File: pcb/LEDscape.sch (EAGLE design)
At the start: 41 parts, among them IC1 MAX3040CSE, IC2 MAX3040CSE, IC3 MAX3040CSE, IC4 MAX3040CSE, IC5 MAX3040CSE, IC6 MAX3040CSE, IC7 MAX3040CSE, IC8 MAX3040CSE

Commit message: Update board to use 2x8 RJ45 connector
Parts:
- removed CN1, CN10, CN11, CN12, CN13, CN14, CN15, CN16, CN17, CN18, CN19, CN2, CN20, CN21, CN22, CN23, CN24, CN25, CN26, CN27, CN28, CN29, CN3, CN30, CN31, CN32, CN4, CN5, CN6, CN7, CN8, CN9: (no value), adafruit:JST_2PIN-SMT
- added U$10, U$3, U$4, U$5, U$6, U$7, U$8, U$9: RJ45_8X2_JACK, LEDscape:RJ45_8X2_JACK
- added U$2: RJ45_8X2_BASE, LEDscape:RJ45_8X2_BASE
- IC1, IC2, IC3, IC4, IC5, IC6, IC7, IC8: value MAX3040CSE -> MAX3041CUE; device maxim:MAX3040CSE -> maxim:MAX3041CUE
- U$1: value BEAGLEBONE_OUTLINE -> BEAGLEBONE_NO_OUTLINE; device adafruit:BEAGLEBONE_OUTLINE -> LEDscape:BEAGLEBONE_NO_OUTLINE
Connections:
- removed net N$57: CN28.1, IC7.Y4
- removed net N$66: CN32.2, IC8.Z4
- new net N$11: IC6.Z2, U$7.P$6
- new net N$14: IC3.Z2, U$5.P$6
- net GND: now also U$10.P$15, U$10.P$16, U$10.P$7, U$10.P$8, U$3.P$15, U$3.P$16, U$3.P$7, U$3.P$8, U$4.P$15, U$4.P$16, U$4.P$7, U$4.P$8, U$5.P$15, U$5.P$16, U$5.P$7, U$5.P$8, U$6.P$15, U$6.P$16, U$6.P$7, U$6.P$8, U$7.P$15, U$7.P$16, U$7.P$7, U$7.P$8, U$8.P$15, U$8.P$16, U$8.P$7, U$8.P$8, U$9.P$15, U$9.P$16, U$9.P$7, U$9.P$8
- net N$1: now also U$3.P$1; no longer CN1.1
- net N$10: now also U$4.P$2; no longer CN5.2
- net N$12: now also U$4.P$3; no longer CN6.1
- net N$13: now also U$4.P$6; no longer CN6.2
- net N$15: now also U$4.P$9; no longer CN7.1
- net N$16: now also U$4.P$10; no longer CN7.2
- net N$17: now also U$4.P$11; no longer CN8.1
- net N$18: now also U$4.P$14; no longer CN8.2
- net N$19: now also U$5.P$1; no longer CN9.1
- net N$2: now also U$3.P$2; no longer CN1.2
- net N$20: now also U$5.P$2; no longer CN9.2
- net N$21: now also U$5.P$3; no longer CN10.1
- net N$22: now also IC3.Z4, U$5.P$14; no longer CN10.2, IC3.Z2
- net N$23: now also U$5.P$9; no longer CN11.1
- net N$24: now also U$5.P$10; no longer CN11.2
- net N$25: now also U$5.P$11; no longer CN12.1
- net N$26: now also IC7.Y2, U$8.P$3; no longer CN12.2, IC3.Z4
- net N$27: now also U$9.P$1; no longer CN13.1
- net N$28: now also U$9.P$2; no longer CN13.2
- net N$29: now also U$9.P$3; no longer CN14.1
- net N$3: now also U$4.P$1; no longer CN5.1
- net N$30: now also U$9.P$6; no longer CN14.2
- net N$31: now also IC4.Z4, U$9.P$14; no longer CN15.1, IC4.Y3
- net N$32: now also U$9.P$10; no longer CN15.2
- net N$33: now also U$9.P$11; no longer CN16.1
- net N$34: now also IC4.Y3, U$9.P$9; no longer CN16.2, IC4.Z4
- net N$35: now also U$6.P$1; no longer CN17.1
- net N$36: now also U$6.P$2; no longer CN17.2
- net N$37: now also U$6.P$3; no longer CN18.1
- net N$38: now also U$6.P$6; no longer CN18.2
- net N$39: now also U$6.P$9; no longer CN19.1
- net N$4: now also U$3.P$3; no longer CN2.1
- net N$40: now also U$6.P$10; no longer CN19.2
- net N$41: now also U$6.P$11; no longer CN20.1
- net N$42: now also U$6.P$14; no longer CN20.2
- net N$43: now also U$7.P$1; no longer CN21.1
- net N$44: now also U$7.P$2; no longer CN21.2
- net N$45: now also U$7.P$3; no longer CN22.1
- net N$46: now also IC7.Z2, U$8.P$6; no longer CN22.2, IC6.Z2
- net N$47: now also U$7.P$9; no longer CN23.1
- net N$48: now also U$7.P$10; no longer CN23.2
- net N$49: now also U$7.P$11; no longer CN24.1
- net N$5: now also U$3.P$6; no longer CN2.2
- net N$50: now also U$7.P$14; no longer CN24.2
- net N$51: now also U$8.P$1; no longer CN25.1
- net N$52: now also U$8.P$2; no longer CN25.2
- net N$53: now also IC7.Y3, U$8.P$9; no longer CN26.1, IC7.Y2
- net N$54: now also IC7.Y4, U$8.P$11; no longer CN26.2, IC7.Z2
- net N$55: now also IC7.Z4, U$8.P$14; no longer CN27.1, IC7.Y3
- net N$56: now also U$8.P$10; no longer CN27.2
- net N$58: now also IC8.Y2, U$10.P$3; no longer CN28.2, IC7.Z4
- net N$59: now also U$10.P$1; no longer CN29.1
- net N$6: now also U$3.P$9; no longer CN3.1
- net N$60: now also U$10.P$2; no longer CN29.2
- net N$61: now also IC8.Z2, U$10.P$6; no longer CN30.1, IC8.Y2
- net N$62: now also IC8.Y4, U$10.P$11; no longer CN30.2, IC8.Z2
- net N$63: now also U$10.P$9; no longer CN31.1
- net N$64: now also U$10.P$10; no longer CN31.2
- net N$65: now also IC8.Z4, U$10.P$14; no longer CN32.1, IC8.Y4
- net N$7: now also U$3.P$10; no longer CN3.2
- net N$8: now also U$3.P$11; no longer CN4.1
- net N$9: now also U$3.P$14; no longer CN4.2
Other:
- moved on the sheet: IC2, IC3, IC4, IC6, IC7, IC8

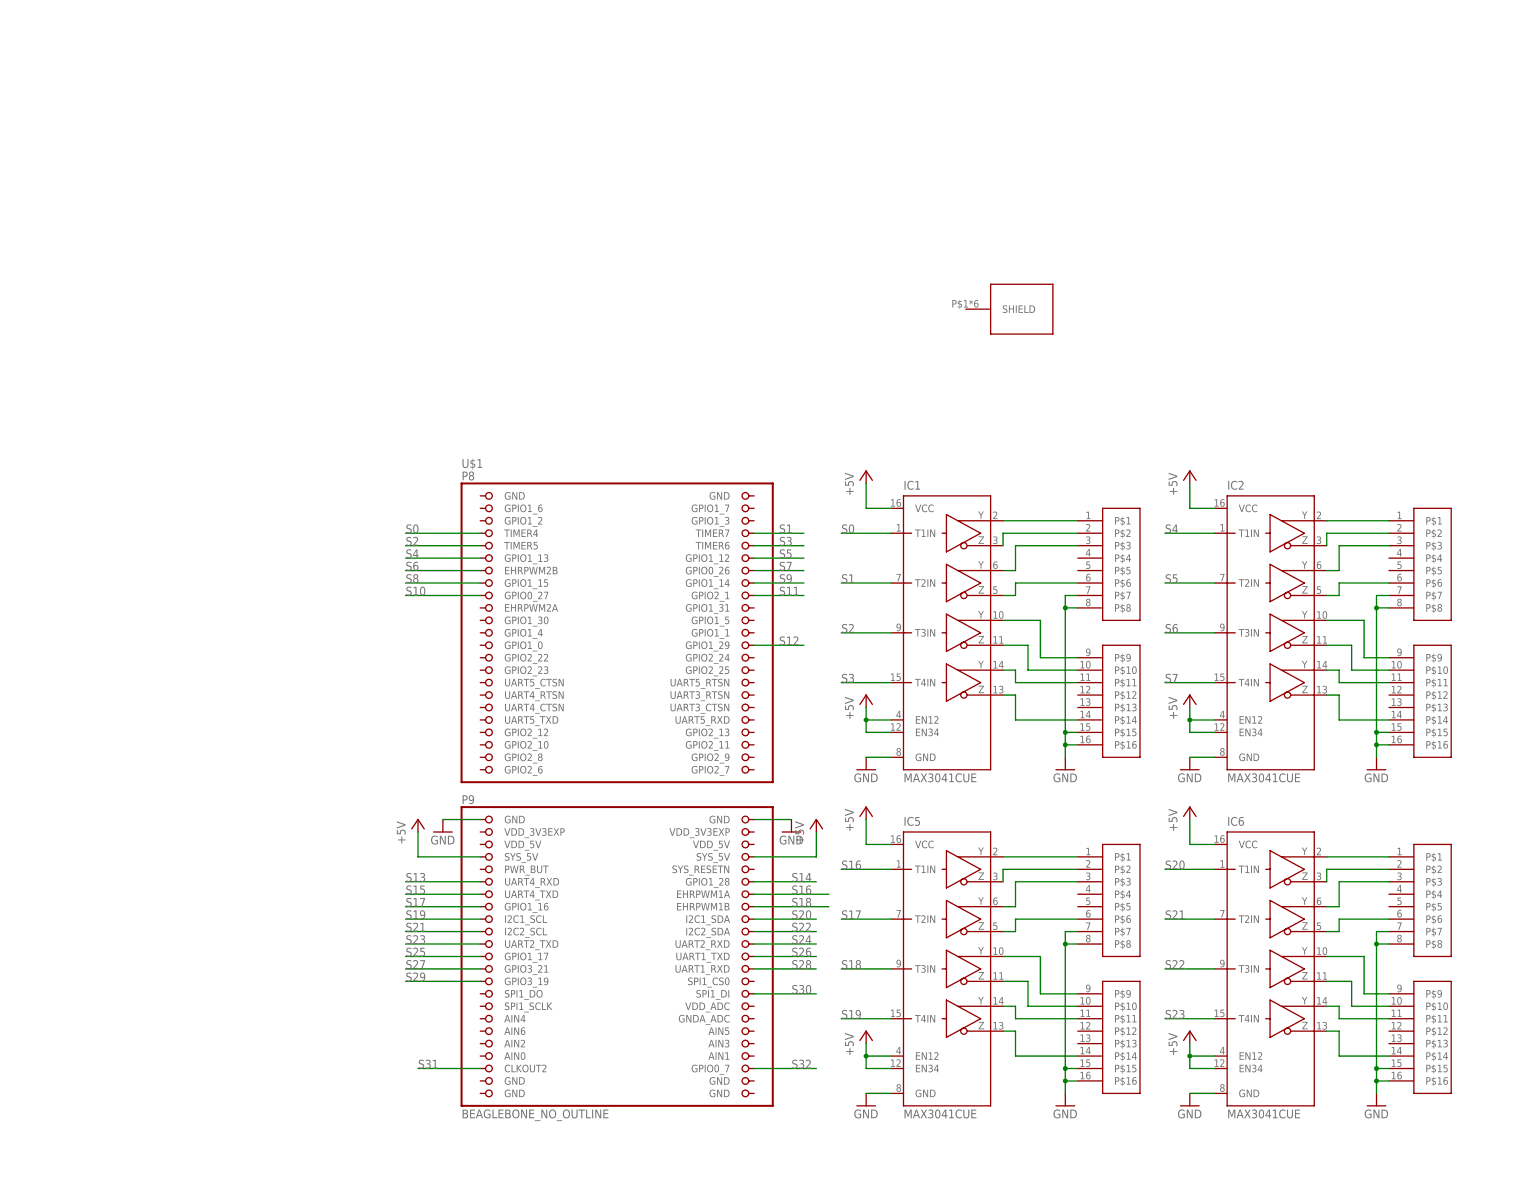
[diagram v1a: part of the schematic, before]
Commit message: Flip board over (put everything on the front, not the back), add caps, work on routing.
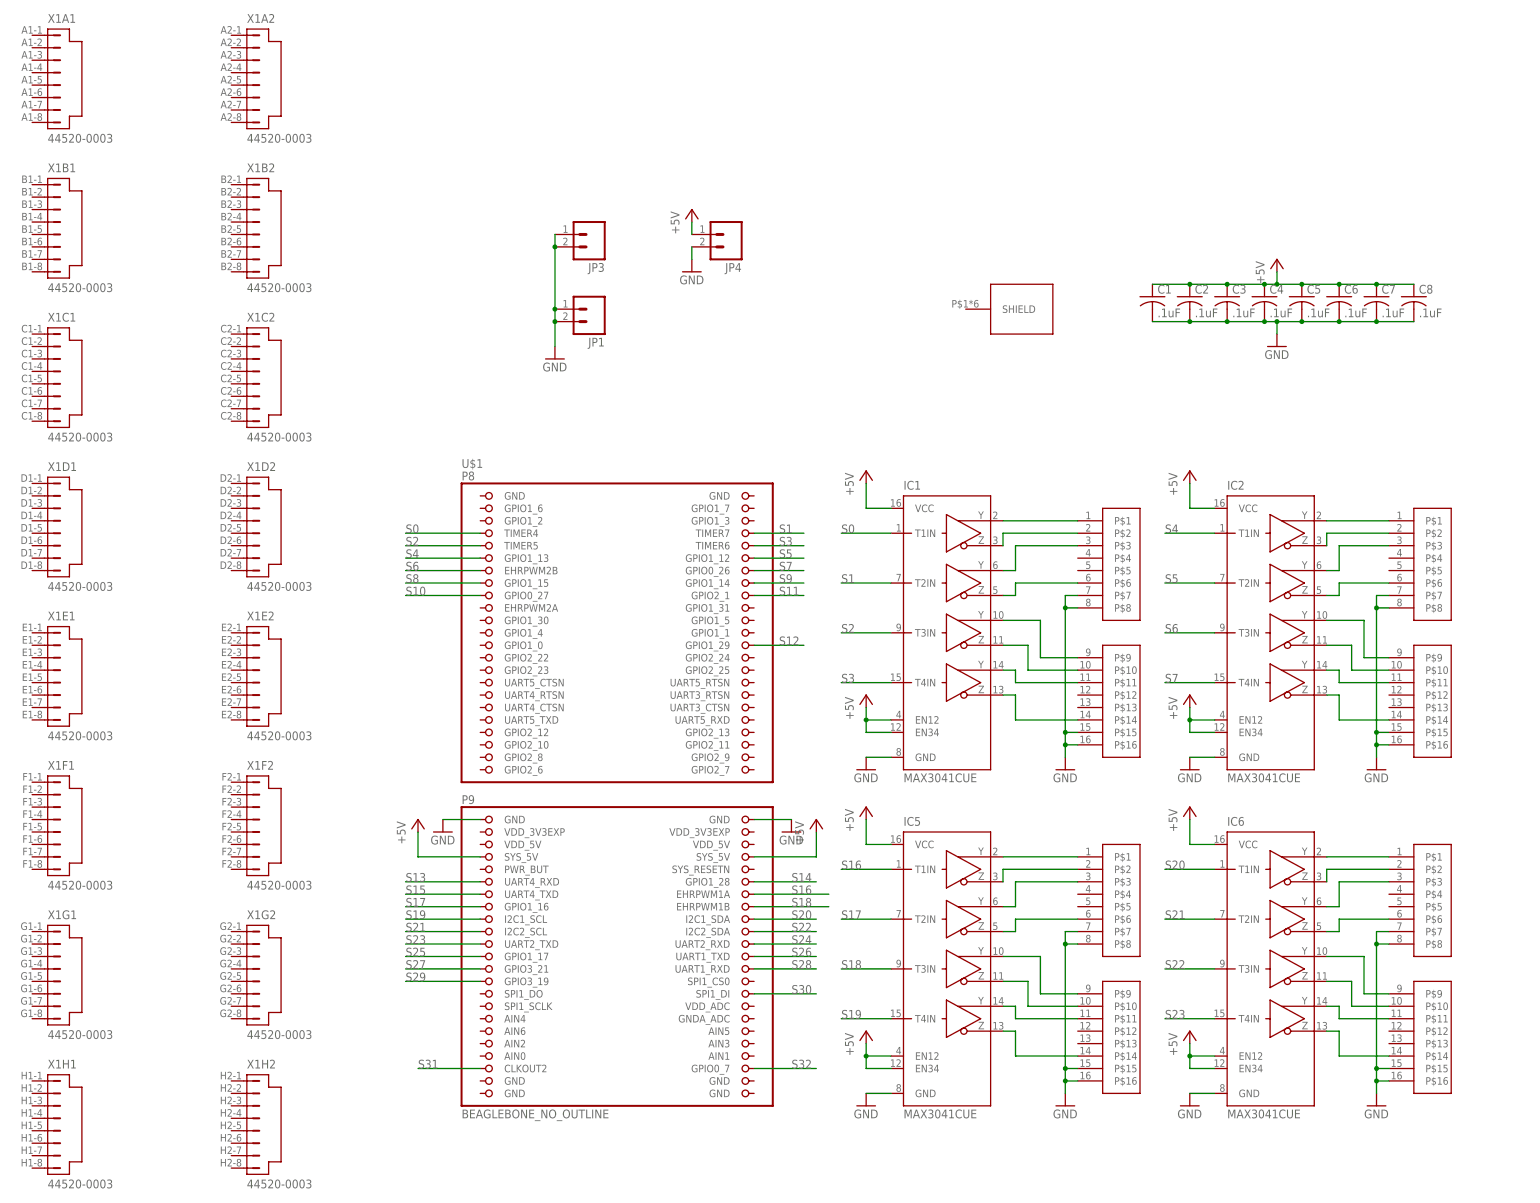
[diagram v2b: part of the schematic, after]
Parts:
- added C1, C2, C3, C4, C5, C6, C7, C8: .1uF, adafruit:C-USC0603
- added JP1, JP3, JP4: (no value), SparkFun-Connectors:M025MM
- added X1: 44520-0003, con-molex:44520-0003
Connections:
- net +5V: now also C1.1, C2.1, C3.1, C4.1, C5.1, C6.1, C7.1, C8.1, JP4.1
- net GND: now also C1.2, C2.2, C3.2, C4.2, C5.2, C6.2, C7.2, C8.2, JP1.1, JP1.2, JP3.1, JP3.2, JP4.2
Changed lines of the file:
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@@
 <part name="GND17" library="supply1" deviceset="GND" device=""/>
 <part name="GND18" library="supply1" deviceset="GND" device=""/>
+<part name="C1" library="adafruit" deviceset="C-US" device="C0603" value=".1uF"/>
+<part name="C2" library="adafruit" deviceset="C-US" device="C0603" value=".1uF"/>
+<part name="C3" library="adafruit" deviceset="C-US" device="C0603" value=".1uF"/>
+<part name="C4" library="adafruit" deviceset="C-US" device="C0603" value=".1uF"/>
+<part name="C5" library="adafruit" deviceset="C-US" device="C0603" value=".1uF"/>
+<part name="C6" library="adafruit" deviceset="C-US" device="C0603" value=".1uF"/>
+<part name="C7" library="adafruit" deviceset="C-US" device="C0603" value=".1uF"/>
+<part name="C8" library="adafruit" deviceset="C-US" device="C0603" value=".1uF"/>
+<part name="P+19" library="supply1" deviceset="+5V" device=""/>
+<part name="GND19" library="supply1" deviceset="GND" device=""/>
+<part name="X1" library="con-molex" deviceset="44520-0003" device=""/>
+<part name="JP1" library="SparkFun-Connectors" deviceset="M02" device="5MM"/>
+<part name="JP3" library="SparkFun-Connectors" deviceset="M02" device="5MM"/>
+<part name="JP4" library="SparkFun-Connectors" deviceset="M02" device="5MM"/>
+<part name="P+20" library="supply1" deviceset="+5V" device=""/>
+<part name="GND20" library="supply1" deviceset="GND" device=""/>
+<part name="GND21" library="supply1" deviceset="GND" device=""/>
 </parts>
 <sheets>
@@
 <instance part="GND17" gate="1" x="370.84" y="-27.94"/>
 <instance part="GND18" gate="1" x="370.84" y="40.64"/>
+<instance part="C1" gate="G$1" x="162.56" y="137.16"/>
+<instance part="C2" gate="G$1" x="170.18" y="137.16"/>
+<instance part="C3" gate="G$1" x="177.8" y="137.16"/>
+<instance part="C4" gate="G$1" x="185.42" y="137.16"/>
+<instance part="C5" gate="G$1" x="193.04" y="137.16"/>
+<instance part="C6" gate="G$1" x="200.66" y="137.16"/>
+<instance part="C7" gate="G$1" x="208.28" y="137.16"/>
+<instance part="C8" gate="G$1" x="215.9" y="137.16"/>
+<instance part="P+19" gate="1" x="187.96" y="144.78"/>
+<instance part="GND19" gate="1" x="187.96" y="127"/>
+<instance part="X1" gate="A1" x="-60.96" y="182.88"/>
+<instance part="X1" gate="A2" x="-20.32" y="182.88"/>
+<instance part="X1" gate="B1" x="-60.96" y="152.4"/>
+<instance part="X1" gate="B2" x="-20.32" y="152.4"/>
+<instance part="X1" gate="C1" x="-60.96" y="121.92"/>
+<instance part="X1" gate="C2" x="-20.32" y="121.92"/>
+<instance part="X1" gate="D1" x="-60.96" y="91.44"/>
+<instance part="X1" gate="D2" x="-20.32" y="91.44"/>
+<instance part="X1" gate="E1" x="-60.96" y="60.96"/>
+<instance part="X1" gate="E2" x="-20.32" y="60.96"/>
+<instance part="X1" gate="F1" x="-60.96" y="30.48"/>
+<instance part="X1" gate="F2" x="-20.32" y="30.48"/>
+<instance part="X1" gate="G1" x="-60.96" y="0"/>
+<instance part="X1" gate="G2" x="-20.32" y="0"/>
+<instance part="X1" gate="H1" x="-60.96" y="-30.48"/>
+<instance part="X1" gate="H2" x="-20.32" y="-30.48"/>
+<instance part="JP1" gate="G$1" x="48.26" y="134.62" rot="R180"/>
+<instance part="JP3" gate="G$1" x="48.26" y="149.86" rot="R180"/>
+<instance part="JP4" gate="G$1" x="76.2" y="149.86" rot="R180"/>
+<instance part="P+20" gate="1" x="68.58" y="154.94"/>
+<instance part="GND20" gate="1" x="68.58" y="142.24"/>
+<instance part="GND21" gate="1" x="40.64" y="124.46"/>
 </instances>
 <busses>
@@
 <junction x="332.74" y="-17.78"/>
 <pinref part="P+18" gate="1" pin="+5V"/>
+</segment>
+<segment>
+<pinref part="C1" gate="G$1" pin="1"/>
+<pinref part="C2" gate="G$1" pin="1"/>
+<wire x1="162.56" y1="139.7" x2="170.18" y2="139.7" width="0.1524" layer="91"/>
+<pinref part="C3" gate="G$1" pin="1"/>
+<wire x1="170.18" y1="139.7" x2="177.8" y2="139.7" width="0.1524" layer="91"/>
+<pinref part="C4" gate="G$1" pin="1"/>
+<wire x1="177.8" y1="139.7" x2="185.42" y2="139.7" width="0.1524" layer="91"/>
+<pinref part="C5" gate="G$1" pin="1"/>
+<wire x1="185.42" y1="139.7" x2="187.96" y2="139.7" width="0.1524" layer="91"/>
+<pinref part="C6" gate="G$1" pin="1"/>
+<wire x1="187.96" y1="139.7" x2="193.04" y2="139.7" width="0.1524" layer="91"/>
+<wire x1="193.04" y1="139.7" x2="200.66" y2="139.7" width="0.1524" layer="91"/>
+<pinref part="C7" gate="G$1" pin="1"/>
+<wire x1="200.66" y1="139.7" x2="208.28" y2="139.7" width="0.1524" layer="91"/>
+<pinref part="C8" gate="G$1" pin="1"/>
+<wire x1="208.28" y1="139.7" x2="215.9" y2="139.7" width="0.1524" layer="91"/>
+<wire x1="187.96" y1="139.7" x2="187.96" y2="142.24" width="0.1524" layer="91"/>
+<junction x="187.96" y="139.7"/>
+<pinref part="P+19" gate="1" pin="+5V"/>
+<junction x="170.18" y="139.7"/>
+<junction x="177.8" y="139.7"/>
+<junction x="185.42" y="139.7"/>
+<junction x="193.04" y="139.7"/>
+<junction x="200.66" y="139.7"/>
+<junction x="208.28" y="139.7"/>
+</segment>
+<segment>
+<pinref part="JP4" gate="G$1" pin="1"/>
+<wire x1="68.58" y1="149.86" x2="68.58" y2="152.4" width="0.1524" layer="91"/>
+<pinref part="P+20" gate="1" pin="+5V"/>
 </segment>
 </net>
@@
 <junction x="370.84" y="45.72"/>
 </segment>
+<segment>
+<pinref part="C8" gate="G$1" pin="2"/>
+<pinref part="C7" gate="G$1" pin="2"/>
+<wire x1="215.9" y1="132.08" x2="208.28" y2="132.08" width="0.1524" layer="91"/>
+<pinref part="C6" gate="G$1" pin="2"/>
+<wire x1="208.28" y1="132.08" x2="200.66" y2="132.08" width="0.1524" layer="91"/>
+<pinref part="C5" gate="G$1" pin="2"/>
+<wire x1="200.66" y1="132.08" x2="193.04" y2="132.08" width="0.1524" layer="91"/>
+<pinref part="C4" gate="G$1" pin="2"/>
+<wire x1="193.04" y1="132.08" x2="187.96" y2="132.08" width="0.1524" layer="91"/>
+<pinref part="C3" gate="G$1" pin="2"/>
+<wire x1="187.96" y1="132.08" x2="185.42" y2="132.08" width="0.1524" layer="91"/>
+<wire x1="185.42" y1="132.08" x2="177.8" y2="132.08" width="0.1524" layer="91"/>
+<pinref part="C2" gate="G$1" pin="2"/>
+<wire x1="177.8" y1="132.08" x2="170.18" y2="132.08" width="0.1524" layer="91"/>
+<pinref part="C1" gate="G$1" pin="2"/>
+<wire x1="170.18" y1="132.08" x2="162.56" y2="132.08" width="0.1524" layer="91"/>
+<wire x1="187.96" y1="132.08" x2="187.96" y2="129.54" width="0.1524" layer="91"/>
+<junction x="187.96" y="132.08"/>
+<pinref part="GND19" gate="1" pin="GND"/>
+<junction x="208.28" y="132.08"/>
+<junction x="200.66" y="132.08"/>
+<junction x="193.04" y="132.08"/>
+<junction x="185.42" y="132.08"/>
+<junction x="177.8" y="132.08"/>
+<junction x="170.18" y="132.08"/>
+</segment>
+<segment>
+<pinref part="JP4" gate="G$1" pin="2"/>
+<wire x1="68.58" y1="147.32" x2="68.58" y2="144.78" width="0.1524" layer="91"/>
+<pinref part="GND20" gate="1" pin="GND"/>
+</segment>
+<segment>
+<pinref part="JP3" gate="G$1" pin="1"/>
+<pinref part="JP3" gate="G$1" pin="2"/>
+<wire x1="40.64" y1="149.86" x2="40.64" y2="147.32" width="0.1524" layer="91"/>
+<pinref part="JP1" gate="G$1" pin="1"/>
+<wire x1="40.64" y1="147.32" x2="40.64" y2="134.62" width="0.1524" layer="91"/>
+<pinref part="JP1" gate="G$1" pin="2"/>
+<wire x1="40.64" y1="134.62" x2="40.64" y2="132.08" width="0.1524" layer="91"/>
+<junction x="40.64" y="147.32"/>
+<junction x="40.64" y="134.62"/>
+<junction x="40.64" y="132.08"/>
+<wire x1="40.64" y1="132.08" x2="40.64" y2="127" width="0.1524" layer="91"/>
+<pinref part="GND21" gate="1" pin="GND"/>
+</segment>
 </net>

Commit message: Add some expansion IO (conflicts with HDMI, beware), and fix 8x2 header
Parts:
- removed X1: 44520-0003, con-molex:44520-0003
- added JP2: (no value), SparkFun-Connectors:M03PTH
- added U$12: M08X2, SparkFun-Connectors:M08X2
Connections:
- new net E0: U$1.GPIO2_6, U$12.3
- new net E1: U$1.GPIO2_7, U$12.4
- new net E10: U$1.UART4_CTSN, U$12.13
- new net E11: U$1.UART3_CTSN, U$12.14
- new net E2: U$1.GPIO2_8, U$12.5
- new net E3: U$1.GPIO2_9, U$12.6
- new net E4: U$1.GPIO2_10, U$12.7
- new net E5: U$1.GPIO2_11, U$12.8
- new net E6: U$1.GPIO2_12, U$12.9
- new net E7: U$1.GPIO2_13, U$12.10
- new net E8: U$1.UART5_TXD, U$12.11
- new net E9: U$1.UART5_RXD, U$12.12
- new net EXTRA0: JP2.2, U$1.EHRPWM2A
- net +5V: now also JP2.1, U$12.1, U$12.2
- net GND: now also JP2.3, U$12.15, U$12.16
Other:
- moved on the sheet: JP1, JP3, JP4
